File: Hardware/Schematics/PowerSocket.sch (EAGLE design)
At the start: 63 parts, among them U1 ESP-32S

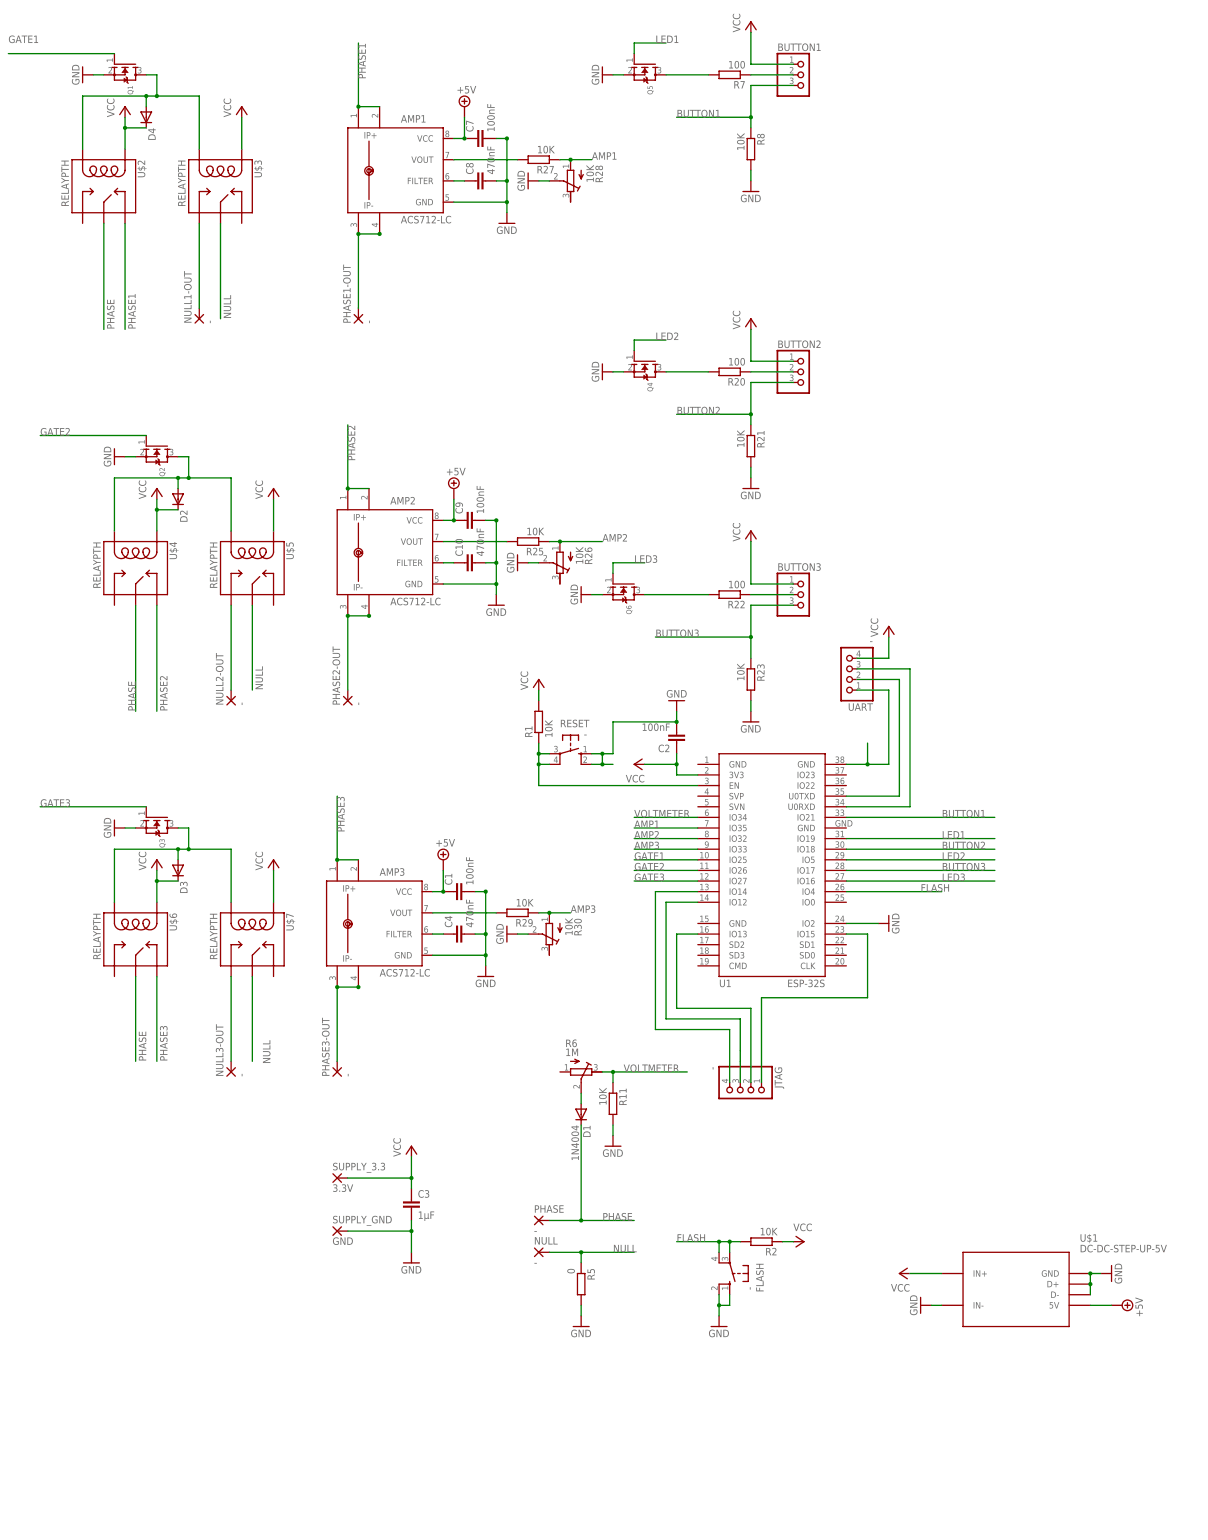
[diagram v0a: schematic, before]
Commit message: Routed power socket board.
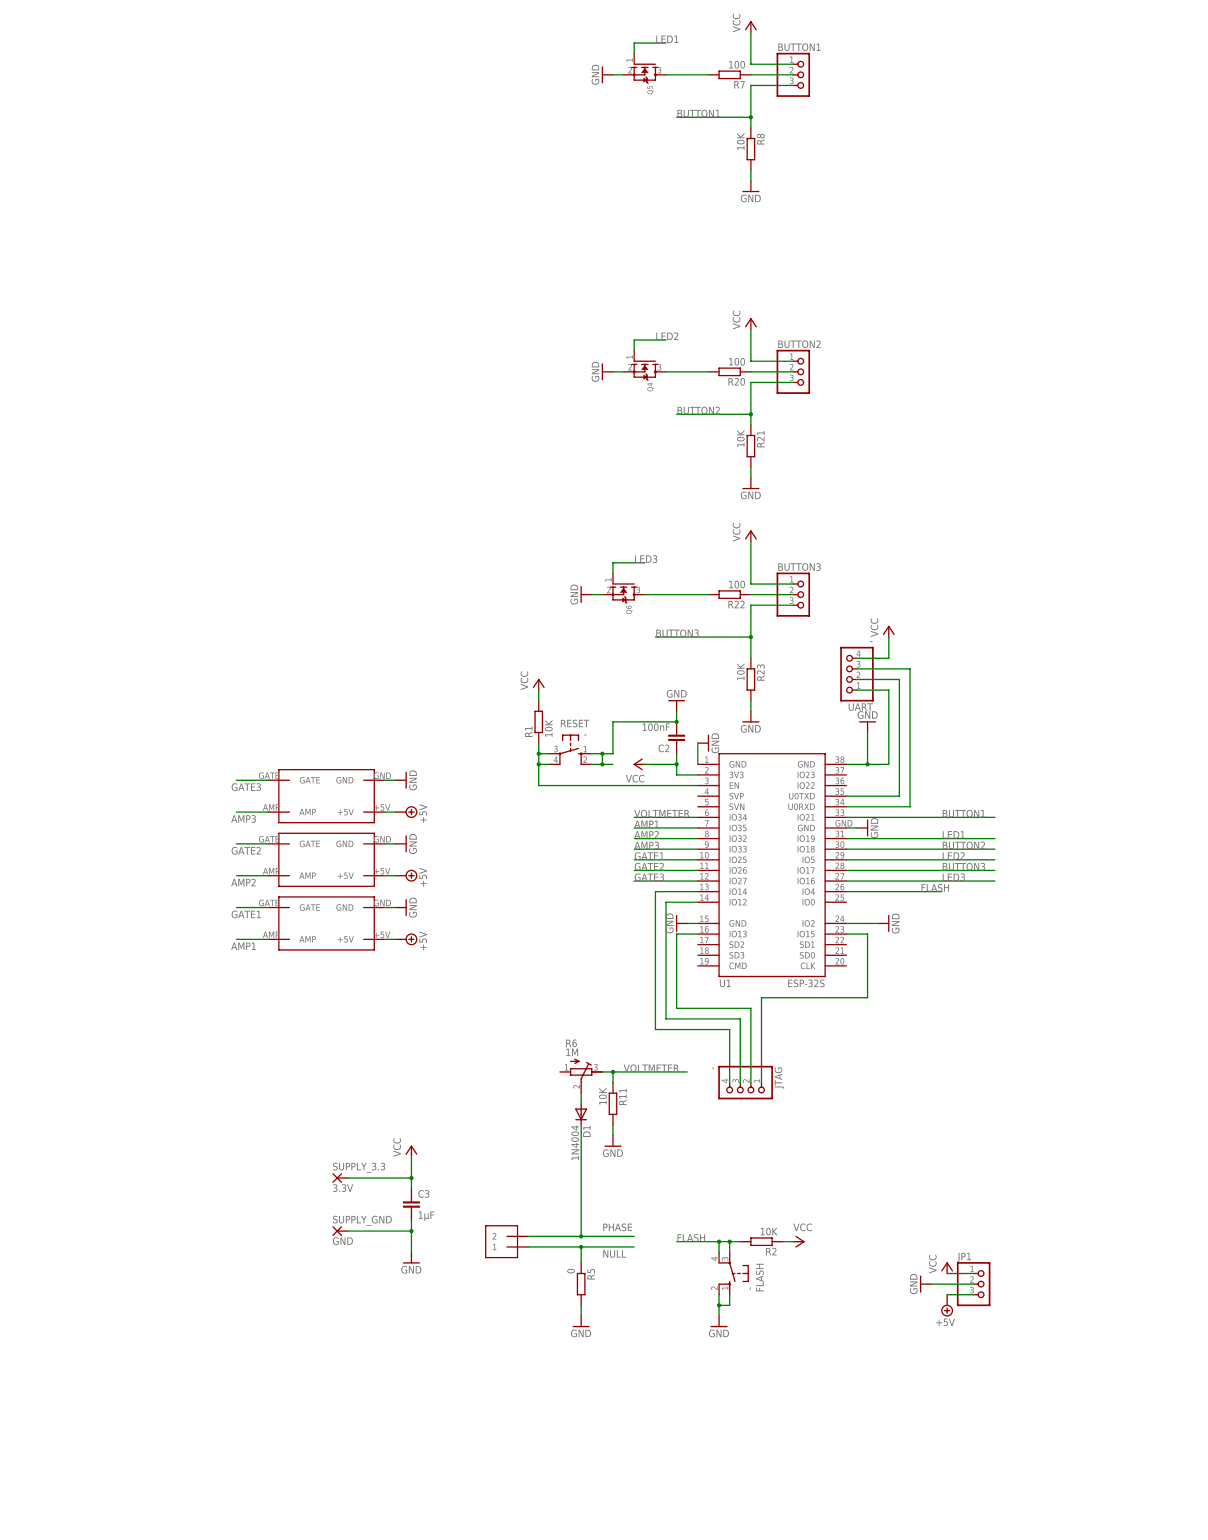
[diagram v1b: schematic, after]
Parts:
- removed AMP1, AMP2, AMP3: ACS712-LC, allegro-2:ACS712-LC
- removed C1, C7, C9: 100nF, rcl:C-EUC0805
- removed C10, C4, C8: 470nF, rcl:C-EUC0805
- removed D2, D3, D4: (no value), diode:DIODE-DO-214AC
- removed NULL, NULL1-OUT, NULL2-OUT, NULL3-OUT, PHASE, PHASE1-OUT, PHASE2-OUT, PHASE3-OUT: -, wirepad:3,81/1,4
- removed Q1, Q2, Q3: (no value), adafruit:MOSFET-NREFLOW
- removed R25, R27, R29: 10K, rcl:R-EU_R0805
- removed R26, R28, R30: 10K, rcl:R-TRIMM5X
- removed U$1: DC-DC-STEP-UP-5V, diy-modules:DC-DC-STEP-UP-5V
- removed U$5, U$6, U$7: RELAYPTH, SRD-05VDC-SL-C:RELAYPTH
- added J2: 1X2-3.5MM, adafruit:1X2-3.5MM
- added JP1: (no value), pinhead:PINHD-1X3
- U$2, U$3, U$4: value RELAYPTH -> RELAY_BOARD; device SRD-05VDC-SL-C:RELAYPTH -> PowerSocket:RELAY_BOARD
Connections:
- removed net N$1: D4.A, Q1.D, U$2.COIL0, U$3.COIL0
- removed net N$10: AMP3.IP-, AMP3.IP-1, PHASE3-OUT.P
- removed net N$12: AMP2.IP-, AMP2.IP-1, PHASE2-OUT.P
- removed net N$13: AMP2.FILTER, C10.1
- removed net N$14: D2.A, Q2.D, U$4.COIL0, U$5.COIL0
- removed net N$17: NULL2-OUT.P, U$5.SWOPEN
- removed net N$19: U1.GND@3, UART.1
- removed net N$24: AMP1.FILTER, C8.1
- removed net N$26: AMP3.FILTER, C4.1
- removed net N$27: AMP1.IP-, AMP1.IP-1, PHASE1-OUT.P
- removed net N$37: AMP3.VOUT, R29.2
- removed net N$39: AMP2.VOUT, R25.2
- removed net N$41: AMP1.VOUT, R27.2
- removed net N$6: D3.A, Q3.D, U$6.COIL0, U$7.COIL0
- removed net N$8: NULL1-OUT.P, U$3.SWOPEN
- removed net NULL_: NULL3-OUT.P, U$7.SWOPEN
- removed net PHASE1: AMP1.IP+, AMP1.IP+1, U$2.SWCLOSE
- removed net PHASE2: AMP2.IP+, AMP2.IP+1, U$4.SWCLOSE
- removed net PHASE3: AMP3.IP+, AMP3.IP+1, U$6.SWCLOSE
- net +5V: now also JP1.3, U$2.+5V, U$3.+5V, U$4.+5V; no longer AMP1.VCC, AMP2.VCC, AMP3.VCC, C1.1, C7.1, C9.1, U$1.5V
- net AMP1: now also U$4.AMP; no longer R27.1, R28.A
- net AMP2: now also U$3.AMP; no longer R25.1, R26.A
- net AMP3: now also U$2.AMP; no longer R29.1, R30.A
- net GATE1: now also U$4.GATE; no longer Q1.G
- net GATE2: now also U$3.GATE; no longer Q2.G
- net GATE3: now also U$2.GATE; no longer Q3.G
- net GND: now also JP1.2, U$2.GND, U$3.GND, U$4.GND, U1.GND@1, U1.GND@2, U1.GND@3, U1.GND@4, UART.1; no longer AMP1.GND, AMP2.GND, AMP3.GND, C1.2, C10.2, C4.2, C7.2, C8.2, C9.2, Q1.S, Q2.S, Q3.S, R26.S, R28.S, R30.S, U$1.D+, U$1.D-, U$1.GND, U$1.IN-
- net NULL: now also J2.1; no longer NULL.P, U$3.SWCOMMON, U$5.SWCOMMON, U$7.SWCOMMON
- net PHASE: now also J2.2; no longer PHASE.P, U$2.SWCOMMON, U$4.SWCOMMON, U$6.SWCOMMON
- net VCC: now also JP1.1; no longer D2.C, D3.C, D4.C, U$1.IN+, U$2.COIL1, U$3.COIL1, U$4.COIL1, U$5.COIL1, U$6.COIL1, U$7.COIL1

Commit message: Added voltage regulators to both boards. Removed solder mask en 220V traces.
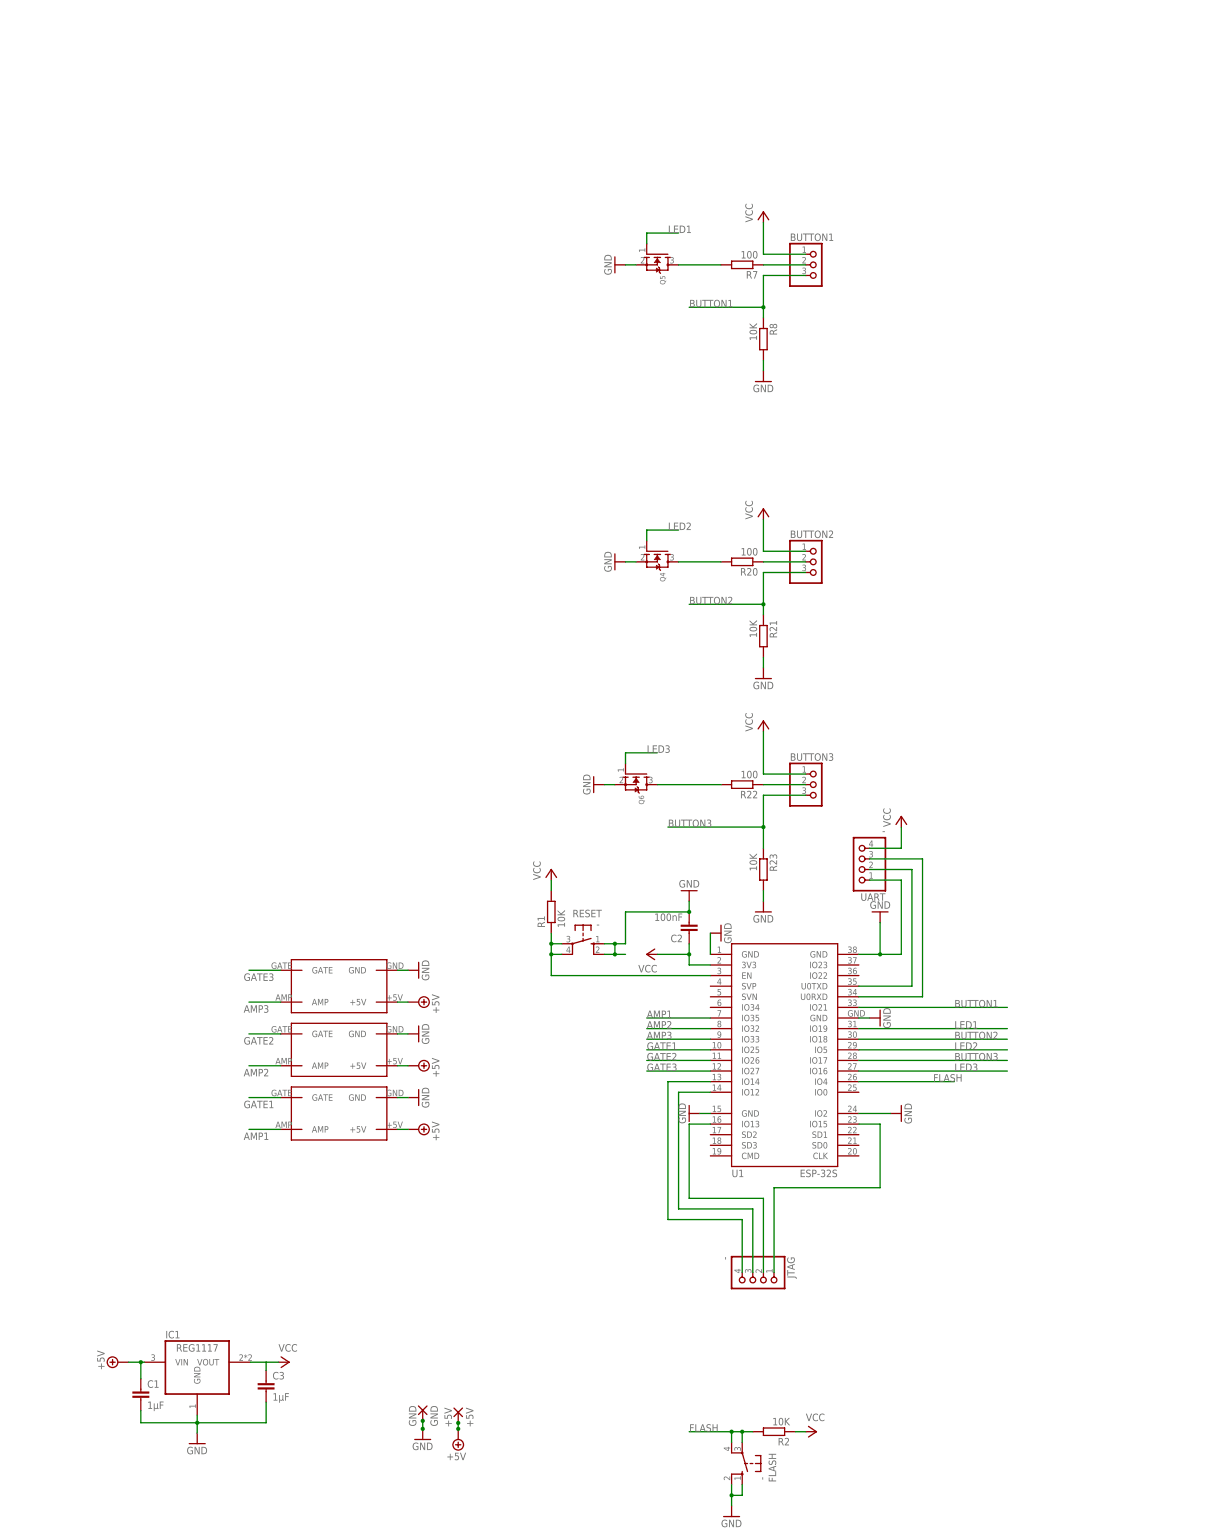
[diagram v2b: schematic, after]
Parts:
- removed D1: 1N4004, diode:1N4004
- removed J2: 1X2-3.5MM, adafruit:1X2-3.5MM
- removed JP1: (no value), pinhead:PINHD-1X3
- removed R11: 10K, rcl:R-EU_R0805
- removed R5: 0, eagle-ltspice:RR2010
- removed R6: 1M, rcl:R-TRIMM3296W
- removed SUPPLY_3.3: 3.3V, wirepad:2,15/1,0
- removed SUPPLY_GND: GND, wirepad:2,15/1,0
- added +5V: +5V, wirepad:2,15/1,0
- added C1: 1µF, rcl:C-EU025-024X044
- added GND: GND, wirepad:2,15/1,0
- added IC1: REG1117, burr-brown:REG1117
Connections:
- removed net N$42: D1.A, R6.S
- removed net NULL: J2.1, R5.1
- removed net PHASE: D1.C, J2.2
- removed net VOLTMETER: R11.1, R6.E, U1.IO34
- net +5V: now also +5V.P, C1.1, IC1.VIN; no longer JP1.3
- net GND: now also C1.2, GND.P, IC1.GND; no longer JP1.2, R11.2, R5.2, SUPPLY_GND.P
- net VCC: now also IC1.VOUT; no longer JP1.1, SUPPLY_3.3.P
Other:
- moved on the sheet: BUTTON1, BUTTON2, BUTTON3, C2, C3, FLASH, JTAG, Q4, Q5, Q6, R1, R2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
